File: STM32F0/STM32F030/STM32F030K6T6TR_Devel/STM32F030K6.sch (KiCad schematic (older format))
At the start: 18 parts, among them J3 Conn_02x10_Odd_Even, J6 Conn_02x05 Odd_Even, SW1 SW_Push, SW2 SW_DIP_x02, U1 STM32F030K6Tx, Y1 8MHz

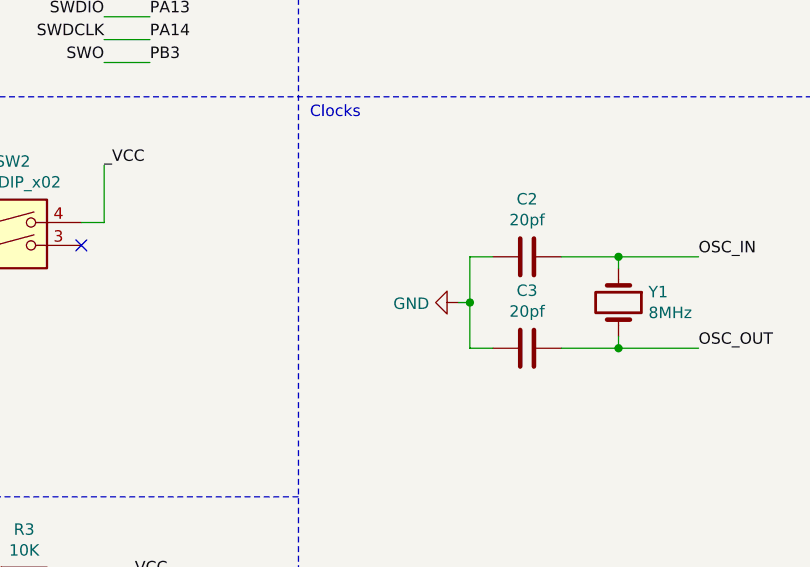
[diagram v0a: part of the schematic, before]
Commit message: Kibot Split on files
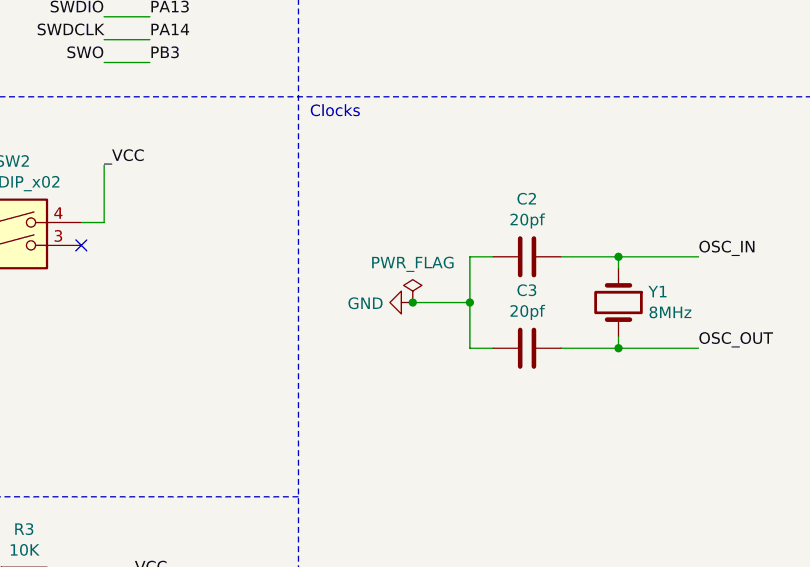
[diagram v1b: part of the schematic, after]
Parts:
- C11, C6, C7: LCSC C49678 -> C49678
- L1: LCSC C1046 -> C1046
- R1, R3: LCSC C17414 -> C17414
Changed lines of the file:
@@
 F 2 "Capacitor_SMD:C_0805_2012Metric" H 2288 1000 50  0001 C CNN
 F 3 "~" H 2250 1150 50  0001 C CNN
-F 4 " C49678" H 2250 1150 50  0001 C CNN "LCSC"
+F 4 "C49678" H 2250 1150 50  0001 C CNN "LCSC"
 	1    2250 1150
 	1    0    0    -1
@@
 F 2 "Capacitor_SMD:C_0805_2012Metric" H 1788 1000 50  0001 C CNN
 F 3 "~" H 1750 1150 50  0001 C CNN
-F 4 " C49678" H 1750 1150 50  0001 C CNN "LCSC"
+F 4 "C49678" H 1750 1150 50  0001 C CNN "LCSC"
 	1    1750 1150
 	1    0    0    -1
@@
 L power:GND #PWR?
 U 1 1 61267F81
-P 7500 3550
+P 7300 3550
 AR Path="/61267F81" Ref="#PWR?"  Part="1"
 AR Path="/6115F145/61267F81" Ref="#PWR01"  Part="1"
-F 0 "#PWR01" H 7500 3300 50  0001 C CNN
-F 1 "GND" V 7505 3422 50  0000 R CNN
-F 2 "" H 7500 3550 50  0001 C CNN
-F 3 "" H 7500 3550 50  0001 C CNN
-	1    7500 3550
+F 0 "#PWR01" H 7300 3300 50  0001 C CNN
+F 1 "GND" V 7305 3422 50  0000 R CNN
+F 2 "" H 7300 3550 50  0001 C CNN
+F 3 "" H 7300 3550 50  0001 C CNN
+	1    7300 3550
 	0    1    1    0
 $EndComp
 Wire Wire Line
-	7500 3550 7550 3550
+	7300 3550 7550 3550
 Wire Wire Line
 	7550 3550 7550 3750
@@
 F 2 "Capacitor_SMD:C_0805_2012Metric" H 4838 4850 50  0001 C CNN
 F 3 "~" H 4800 5000 50  0001 C CNN
-F 4 " C49678" H 4800 5000 50  0001 C CNN "LCSC"
+F 4 "C49678" H 4800 5000 50  0001 C CNN "LCSC"
 	1    4800 5000
 	1    0    0    -1
@@
 F 2 "Resistor_SMD:R_0805_2012Metric" H 4720 3459 50  0001 L CNN
 F 3 "~" H 4650 3550 50  0001 C CNN
-F 4 " C17414" H 4650 3550 50  0001 C CNN "LCSC"
+F 4 "C17414" H 4650 3550 50  0001 C CNN "LCSC"
 	1    4650 3550
 	1    0    0    -1
@@
 F 2 "Resistor_SMD:R_0805_2012Metric" H 5670 4659 50  0001 L CNN
 F 3 "~" H 5600 4750 50  0001 C CNN
-F 4 " C17414" H 5600 4750 50  0001 C CNN "LCSC"
+F 4 "C17414" H 5600 4750 50  0001 C CNN "LCSC"
 	1    5600 4750
 	0    1    1    0
@@
 F 2 "Inductor_SMD:L_0805_2012Metric" H 8250 1350 50  0001 C CNN
 F 3 "~" H 8250 1350 50  0001 C CNN
-F 4 " C1046" V 8250 1350 50  0001 C CNN "LCSC"
+F 4 "C1046" V 8250 1350 50  0001 C CNN "LCSC"
 	1    8250 1350
 	0    1    1    0
@@
 	1    0    0    -1
 $EndComp
+$Comp
+L power:PWR_FLAG #FLG0103
+U 1 1 6125409B
+P 7300 3550
+F 0 "#FLG0103" H 7300 3625 50  0001 C CNN
+F 1 "PWR_FLAG" H 7300 3723 50  0000 C CNN
+F 2 "" H 7300 3550 50  0001 C CNN
+F 3 "~" H 7300 3550 50  0001 C CNN
+	1    7300 3550
+	1    0    0    -1
+$EndComp
+Connection ~ 7300 3550
 $EndSCHEMATC

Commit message: F030K6 Board
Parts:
- removed J3: Conn_02x10_Odd_Even, Connector_PinHeader_2.54mm:PinHeader_2x10_P2.54mm_Vertical, symbol Connector_Generic:Conn_02x10_Odd_Even
- added J3: Conn_01x06, Connector_PinHeader_2.54mm:PinHeader_1x06_P2.54mm_Vertical, symbol Connector_Generic:Conn_01x06
- J6: footprint Connector_PinHeader_1.27mm:PinHeader_2x05_P1.27mm_Vertical -> Connector_PinHeader_1.27mm:PinHeader_2x05_P1.27mm_Vertical_SMD
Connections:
- net GND: now also J3.3 (Pin_3)
- net NRST: now also J3.5 (Pin_5)
- net PA13: now also J3.4 (Pin_4)
- net PA14: now also J3.2 (Pin_2)
- net PB3: now also J3.6 (Pin_6)
- net VCC: now also J3.1 (Pin_1)
- no-connect marks 9 -> 4
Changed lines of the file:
@@
 	3350 500  3350 5600
-$Comp
-L Connector_Generic:Conn_02x10_Odd_Even J?
-U 1 1 612C8F68
-P 4350 1500
-AR Path="/612C8F68" Ref="J?"  Part="1"
-AR Path="/6115F145/612C8F68" Ref="J3"  Part="1"
-F 0 "J3" H 4400 2117 50  0000 C CNN
-F 1 "Conn_02x10_Odd_Even" H 4400 2026 50  0000 C CNN
-F 2 "Connector_PinHeader_2.54mm:PinHeader_2x10_P2.54mm_Vertical" H 4350 1500 50  0001 C CNN
-F 3 "~" H 4350 1500 50  0001 C CNN
-	1    4350 1500
-	1    0    0    -1
-$EndComp
 $Comp
 L power:GND #PWR?
 U 1 1 612C8F6E
-P 4800 2200
+P 3700 1450
 AR Path="/612C8F6E" Ref="#PWR?"  Part="1"
 AR Path="/6115F145/612C8F6E" Ref="#PWR030"  Part="1"
-F 0 "#PWR030" H 4800 1950 50  0001 C CNN
-F 1 "GND" H 4805 2027 50  0000 C CNN
-F 2 "" H 4800 2200 50  0001 C CNN
-F 3 "" H 4800 2200 50  0001 C CNN
-	1    4800 2200
-	1    0    0    -1
-$EndComp
-Wire Wire Line
-	4650 1200 4800 1200
-Wire Wire Line
-	4800 1200 4800 1300
-Wire Wire Line
-	4650 1100 4800 1100
-Wire Wire Line
-	4800 1100 4800 900
-Wire Wire Line
-	3900 1100 3900 900
-Wire Wire Line
-	4650 1300 4800 1300
-Connection ~ 4800 1300
-Wire Wire Line
-	4800 1300 4800 1400
-Wire Wire Line
-	4650 1400 4800 1400
-Connection ~ 4800 1400
-Wire Wire Line
-	4650 1500 4800 1500
-Wire Wire Line
-	4800 1400 4800 1500
-Connection ~ 4800 1500
-Wire Wire Line
-	4800 1500 4800 1600
-Connection ~ 4800 1600
-Wire Wire Line
-	4800 1600 4800 1700
-Wire Wire Line
-	4650 1600 4800 1600
-Wire Wire Line
-	4650 1700 4800 1700
-Connection ~ 4800 1700
-Wire Wire Line
-	4800 1700 4800 1800
-Wire Wire Line
-	4650 1800 4800 1800
-Connection ~ 4800 1800
-Wire Wire Line
-	4800 1800 4800 1900
-Wire Wire Line
-	4650 1900 4800 1900
-Connection ~ 4800 1900
-Wire Wire Line
-	4800 1900 4800 2000
-Wire Wire Line
-	4650 2000 4800 2000
-Connection ~ 4800 2000
-Wire Wire Line
-	4800 2000 4800 2200
-Wire Wire Line
-	3900 1100 4150 1100
-NoConn ~ 4150 1200
-NoConn ~ 4150 1300
-NoConn ~ 4150 1600
-NoConn ~ 4150 1900
-NoConn ~ 4150 2000
-Text Label 3850 1800 2    50   ~ 0
+F 0 "#PWR030" H 3700 1200 50  0001 C CNN
+F 1 "GND" H 3705 1277 50  0000 C CNN
+F 2 "" H 3700 1450 50  0001 C CNN
+F 3 "" H 3700 1450 50  0001 C CNN
+	1    3700 1450
+	1    0    0    -1
+$EndComp
+Wire Wire Line
+	4300 1250 4300 1050
+Wire Wire Line
+	4300 1250 4550 1250
+Text Label 4250 1650 2    50   ~ 0
 RST
 Wire Wire Line
-	3850 1800 4150 1800
-Text Label 3850 1500 2    50   ~ 0
+	4250 1650 4550 1650
+Text Label 4250 1350 2    50   ~ 0
 SWDCLK
-Text Label 3850 1400 2    50   ~ 0
+Text Label 4250 1550 2    50   ~ 0
 SWDIO
 Wire Wire Line
-	3850 1400 4150 1400
-Wire Wire Line
-	4150 1500 3850 1500
-Text Label 3850 1700 2    50   ~ 0
+	4250 1550 4550 1550
+Wire Wire Line
+	4550 1350 4250 1350
+Text Label 4250 1750 2    50   ~ 0
 SWO
 Wire Wire Line
-	3850 1700 4150 1700
+	4250 1750 4550 1750
 $Comp
 L Connector_Generic:Conn_02x05_Odd_Even J?
@@
 F 0 "J6" H 6150 2117 50  0000 C CNN
 F 1 "Conn_02x05 Odd_Even" H 6150 2026 50  0000 C CNN
-F 2 "Connector_PinHeader_1.27mm:PinHeader_2x05_P1.27mm_Vertical" H 6100 1500 50  0001 C CNN
+F 2 "Connector_PinHeader_1.27mm:PinHeader_2x05_P1.27mm_Vertical_SMD" H 6100 1500 50  0001 C CNN
 F 3 "~" H 6100 1500 50  0001 C CNN
 	1    6100 1500
@@
 Text Label 5650 1150 2    50   ~ 0
 _VCC
-Text Label 4800 900  0    50   ~ 0
-_VCC
-Text Label 3900 900  2    50   ~ 0
+Text Label 4300 1050 2    50   ~ 0
 _VCC
 Text HLabel 7800 700  0    50   Input ~ 0
@@
 $EndComp
 Connection ~ 7300 3550
+$Comp
+L Connector_Generic:Conn_01x06 J3
+U 1 1 61316A9B
+P 4750 1450
+F 0 "J3" H 4830 1442 50  0000 L CNN
+F 1 "Conn_01x06" H 4830 1351 50  0000 L CNN
+F 2 "Connector_PinHeader_2.54mm:PinHeader_1x06_P2.54mm_Vertical" H 4750 1450 50  0001 C CNN
+F 3 "~" H 4750 1450 50  0001 C CNN
+	1    4750 1450
+	1    0    0    -1
+$EndComp
+Wire Wire Line
+	3700 1450 4550 1450
 $EndSCHEMATC
